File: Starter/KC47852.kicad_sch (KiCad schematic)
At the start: 49 parts, among them J1 AudioJack, J2 Speaker, J3 UART1, J4 Pot, J6 GND, J7 DACOUT, SW1 UP, SW2 LEFT, SW3 DOWN, SW4 RGHT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

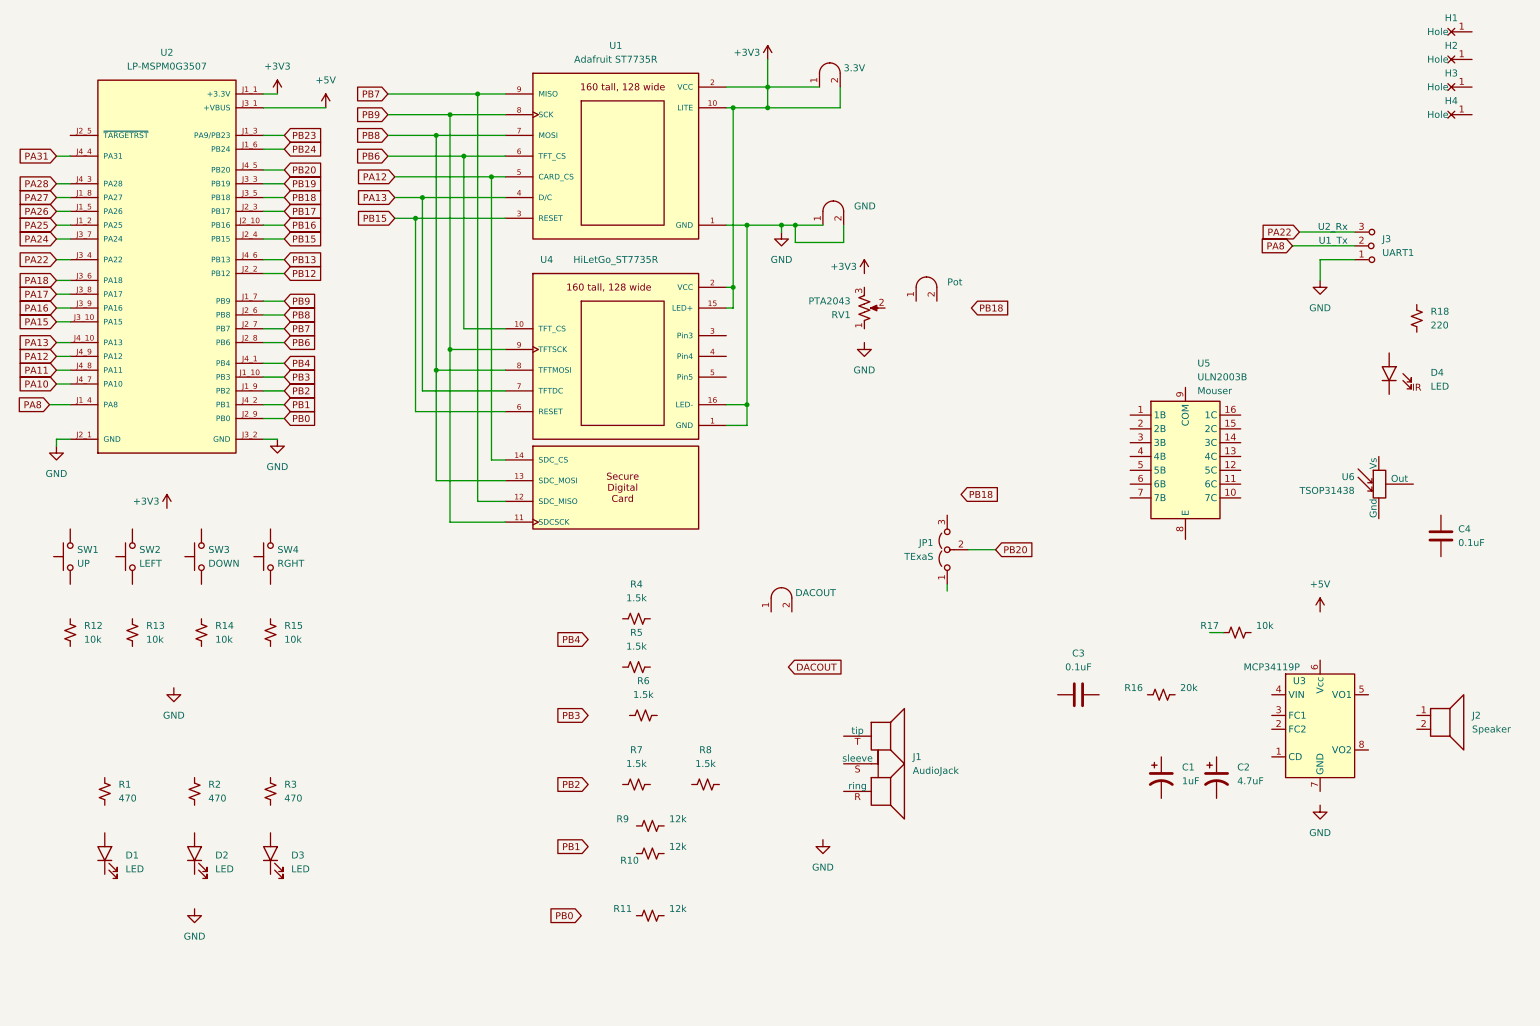
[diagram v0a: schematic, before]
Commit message: Wired LEDs, Switches, DAC, and Jumper
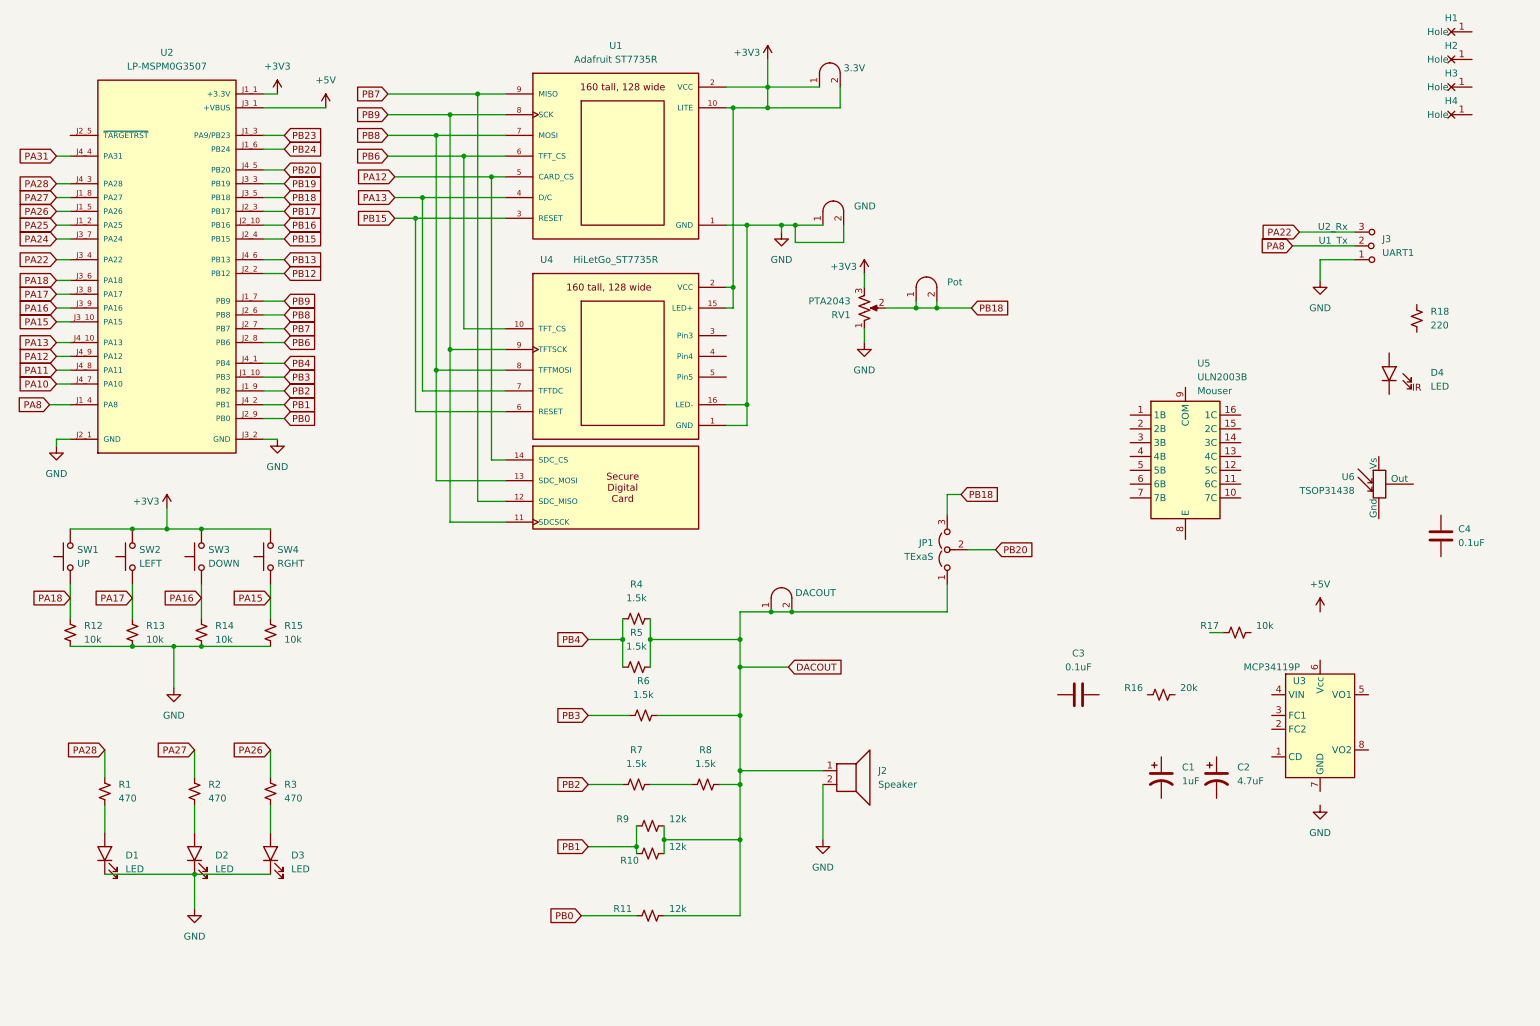
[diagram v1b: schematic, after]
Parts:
- removed J1: AudioJack, ECE319K:Jack_3.5mm_CUI_SJ1-3523N_Horizontal, symbol ECE319K:HeadphoneJack
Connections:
- net +3V3: now also RV1.3, SW1.2, SW2.2, SW3.2, SW4.2
- net DACOUT: now also J2.1, J7.1 (A), J7.2 (B), JP1.1 (A), R10.1, R11.1, R4.1, R5.1, R6.1, R8.1, R9.1
- net GND: now also D1.1 (K), D2.1 (K), D3.1 (K), J2.2, R12.2, R13.2, R14.2, R15.2, RV1.1
- net PA15: now also R15.1, SW4.1
- net PA16: now also R14.1, SW3.1
- net PA17: now also R13.1, SW2.1
- net PA18: now also R12.1, SW1.1
- net PA26: now also R3.1
- net PA27: now also R2.1
- net PA28: now also R1.1
- net PB0: now also R11.2
- net PB1: now also R10.2, R9.2
- net PB18: now also J4.1 (A), J4.2 (B), JP1.3 (B), RV1.2
- net PB2: now also R7.2
- net PB3: now also R6.2
- net PB4: now also R4.2, R5.2
- net at R7.1: now also R8.2
- net at R1.2: now also D1.2 (A)
- net at D3.2 (A): now also R3.2
- net at D2.2 (A): now also R2.2
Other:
- moved on the sheet: J2

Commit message: 319H Components
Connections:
- net +3V3: now also C4.1, U6.2 (Vs)
- net +5V: now also R18.1, U3.6 (Vcc)
- net GND: now also U3.7 (GND), U5.8 (E)
- net PA22: now also U6.3 (Out)
- net PA8: now also U5.1 (1B)
- net at C4.2: now also U6.1 (Gnd)
- net at D4.1 (K): now also U5.16 (1C)
- net at D4.2 (A): now also R18.2
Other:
- moved on the sheet: C4, D4, R18

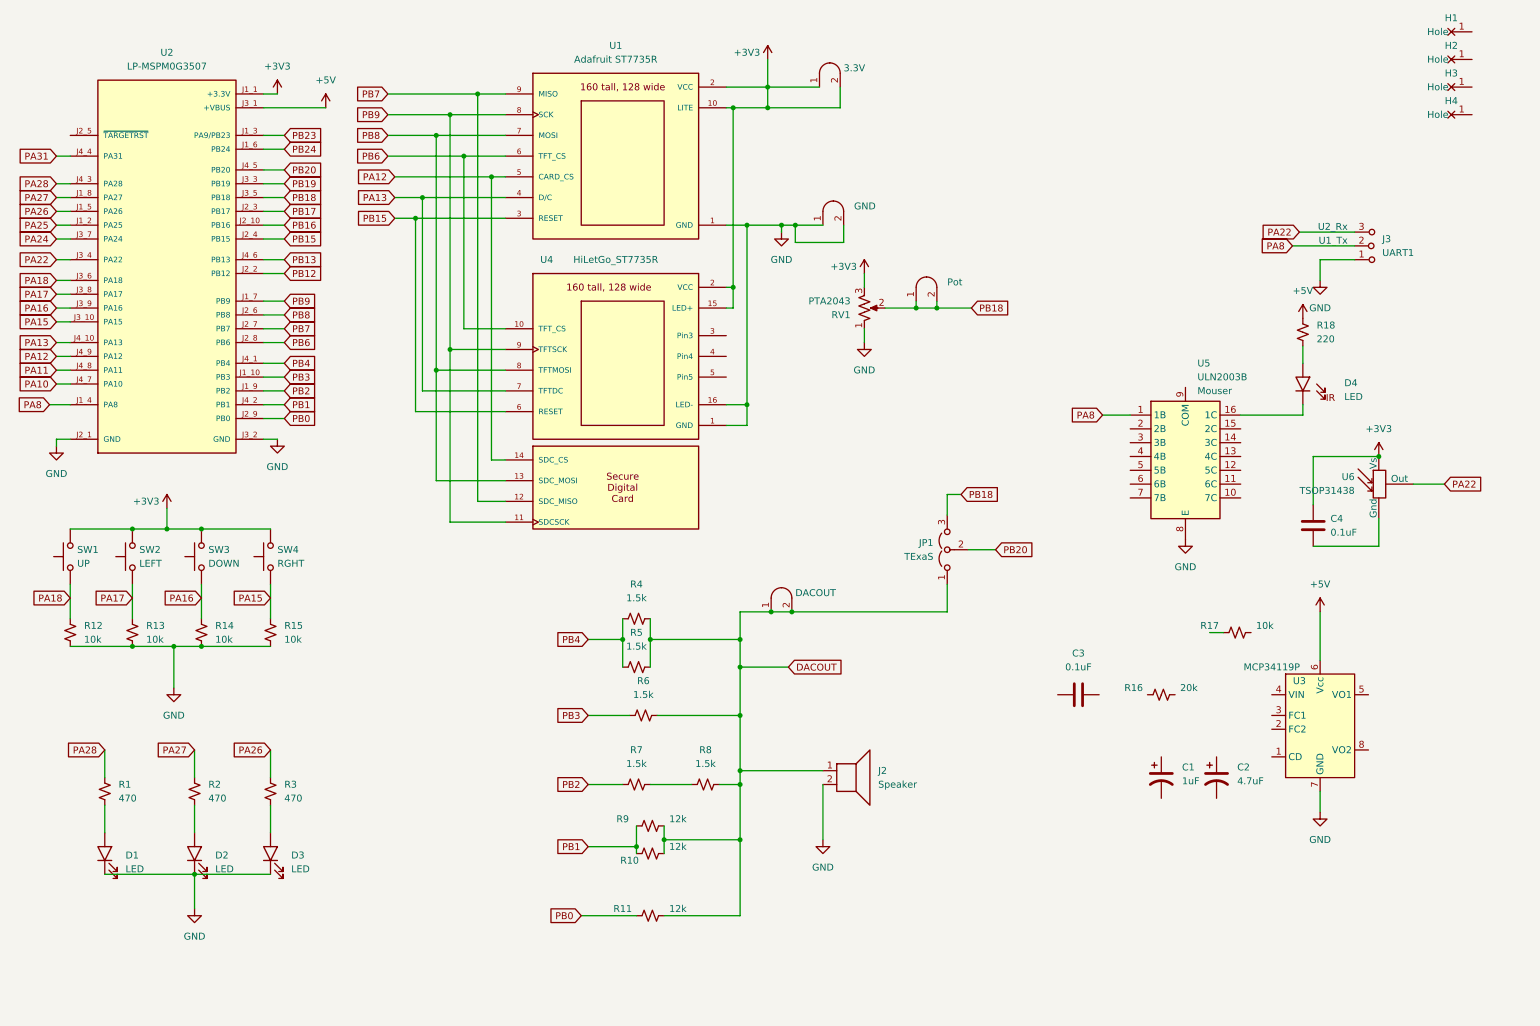
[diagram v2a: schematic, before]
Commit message: Wired audio amplifier. Referenced page 8 of Datasheet. PLEASE DOUBLE CHECK WORK
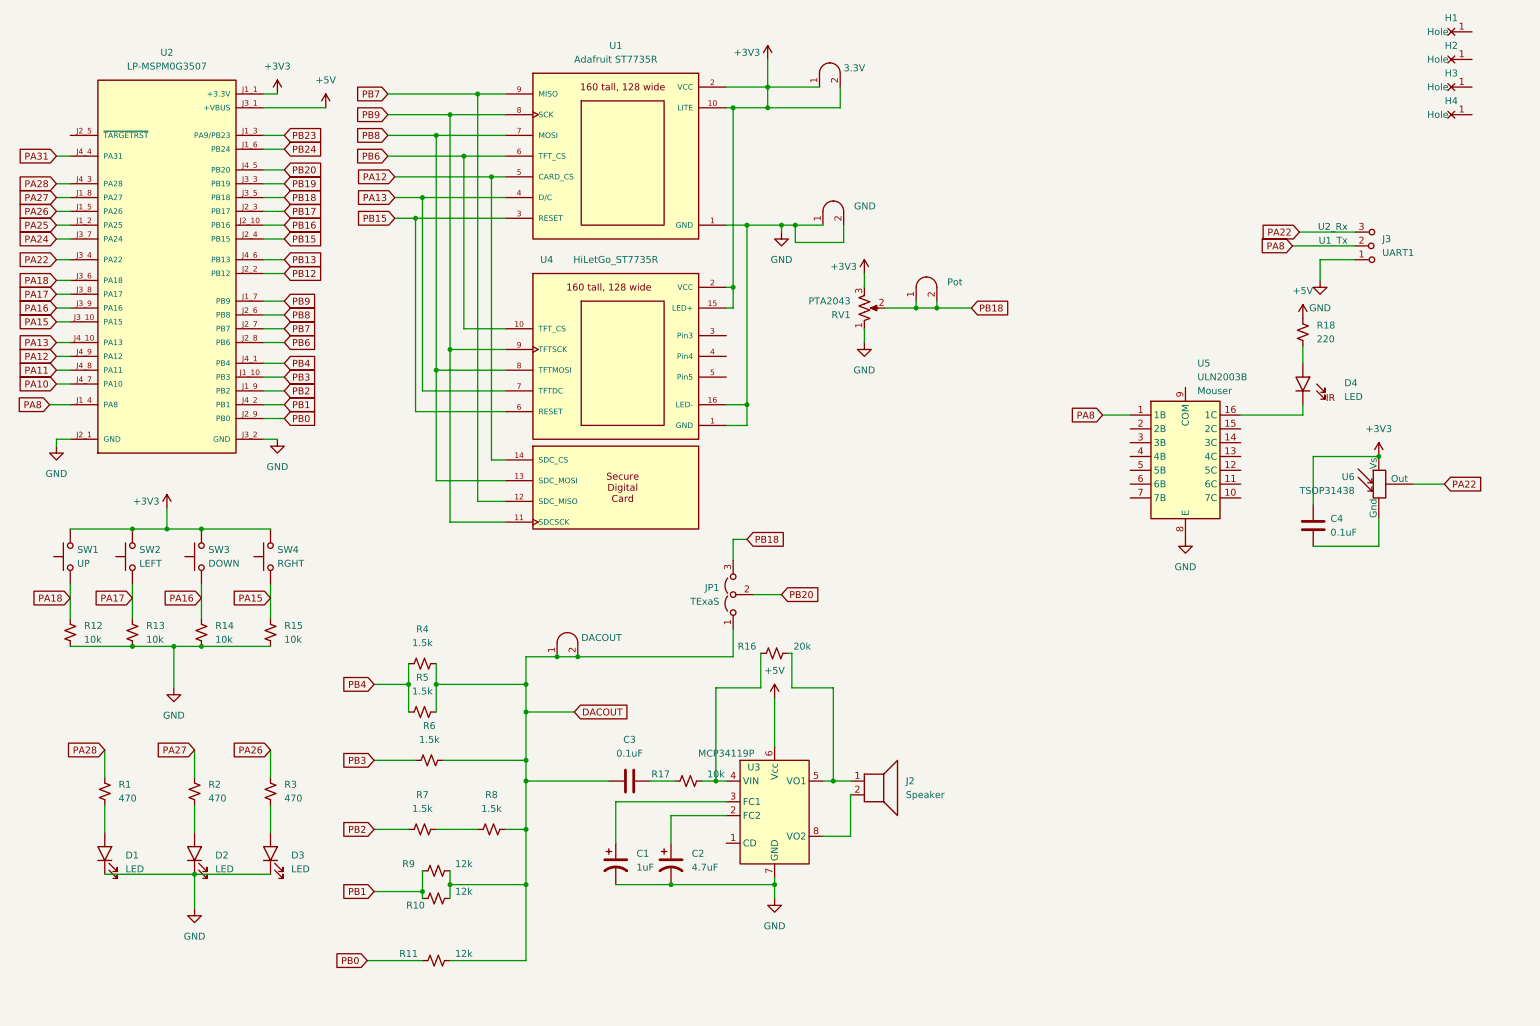
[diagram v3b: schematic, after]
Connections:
- net DACOUT: now also C3.1; no longer J2.1
- net GND: now also C1.2, C2.2; no longer J2.2
- net at U3.2 (FC2): now also C2.1
- net at U3.3 (FC1): now also C1.1
- net at U3.4 (VIN): now also R16.2, R17.1
- net at U3.5 (VO1): now also J2.1, R16.1
- net at U3.8 (VO2): now also J2.2
- net at R17.2: now also C3.2
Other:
- moved on the sheet: C1, C2, C3, J2, JP1, R10, R11, R16, R17, R4, R5, R6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

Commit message: Reformatting and added cross-board wiring as well as IMU
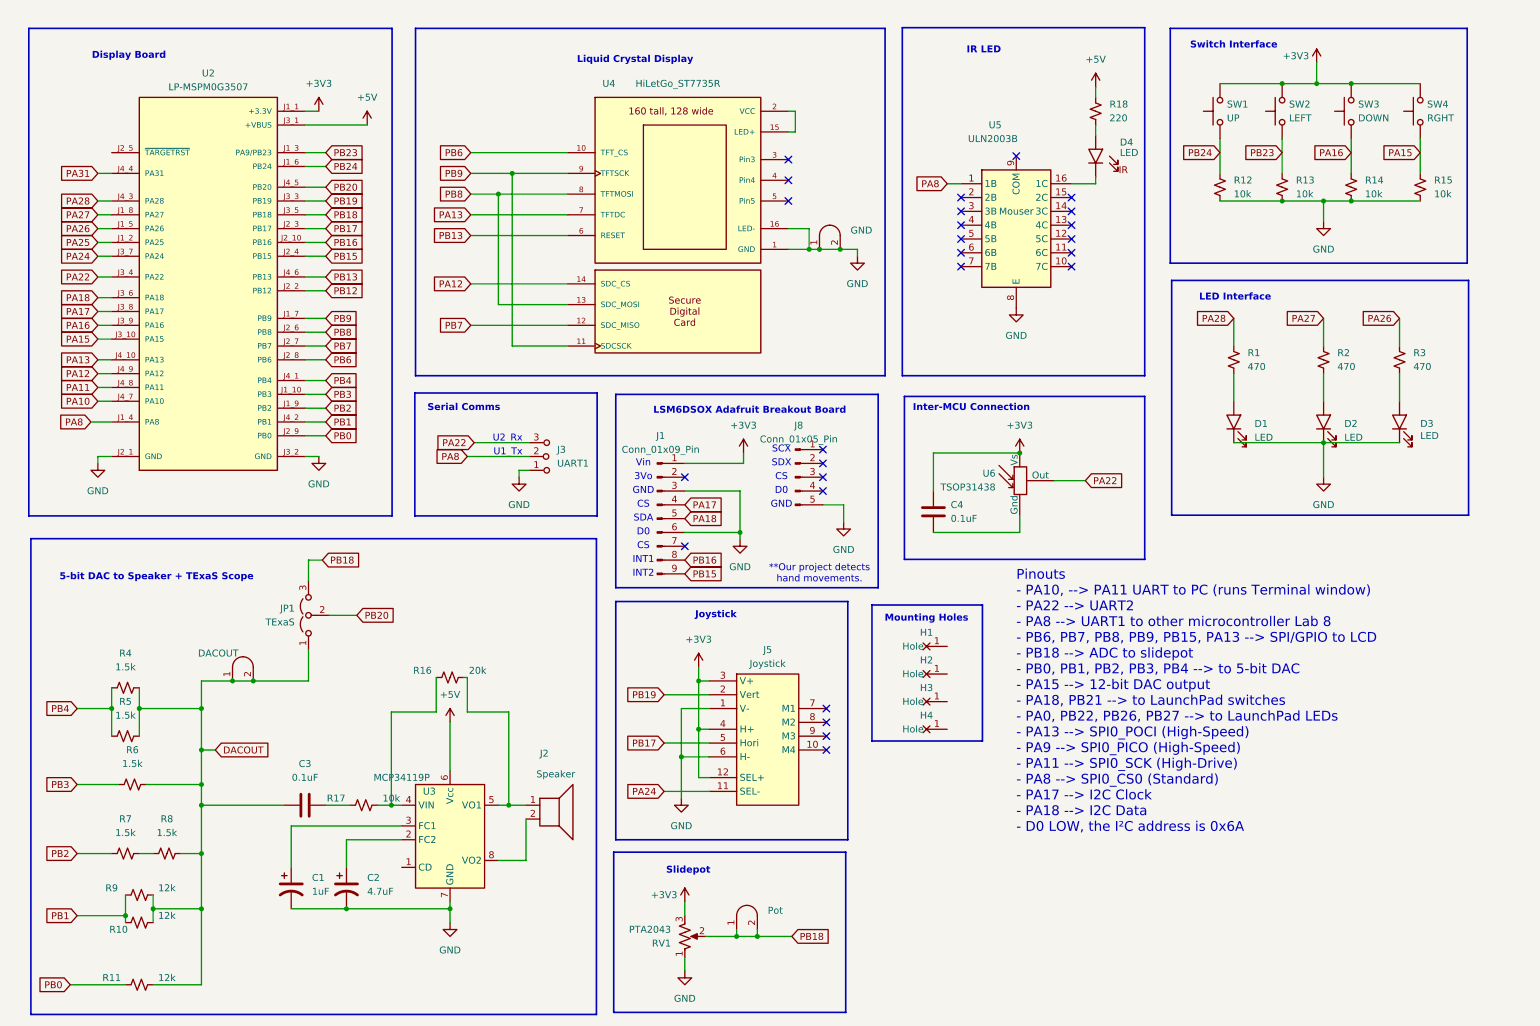
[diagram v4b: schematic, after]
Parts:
- removed TP1: 3.3V, ECE319K:Testpoint_1x02_P2.54mm, symbol ECE319K:Testpoint
- removed U1: Adafruit ST7735R, ECE319K:adafruit_st7735r, symbol ECE319K:Adafruit_ST7735R
- added J1: Conn_01x09_Pin, symbol Connector:Conn_01x09_Pin
- added J5: Joystick, ECE319K:SparkfunJoystick, symbol ECE319H:Joystick_Sparkfun_COM-09032
- added J8: Conn_01x05_Pin, symbol Connector:Conn_01x05_Pin
- U2: symbol ECE319K:LP-MSPM0G3507 -> ECE319H:LP-MSPM0G3507
- U4: symbol ECE319K:HiLetGo_ST7735R -> ECE319H:HiLetGo_ST7735R
- U5: footprint ECE319K:DIP-16_W7.62mm -> ECE319H:DIP-16_W7.62mm; symbol ECE319K:ULN2003B -> ECE319H:ULN2003B
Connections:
- net +3V3: now also J1.1 (Pin_1), J5.12 (SEL+), J5.3 (V+), J5.4 (H+); no longer U4.15 (LED+), U4.2 (VCC)
- net GND: now also J1.3 (Pin_3), J1.6 (Pin_6), J5.1 (V-), J5.6 (H-), J8.5 (Pin_5)
- net PA17: now also J1.4 (Pin_4); no longer R13.1, SW2.1
- net PA18: now also J1.5 (Pin_5); no longer R12.1, SW1.1
- net PA24: now also J5.11 (SEL-)
- net PB13: now also U4.6 (RESET)
- net PB15: now also J1.9 (Pin_9); no longer U4.6 (RESET)
- net PB16: now also J1.8 (Pin_8)
- net PB17: now also J5.5 (Hori)
- net PB19: now also J5.2 (Vert)
- net PB23: now also R13.1, SW2.1
- net PB24: now also R12.1, SW1.1
- new net: U4.15 (LED+), U4.2 (VCC)
- no-connect marks 0 -> 26
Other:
- note added: "**Our project detects hand movements."
- note added: "3Vo"
- note added: "5-bit DAC to Speaker + TExaS Scope"
- note added: "CS"
- note added: "D0"
- note added: "Display Board"
- note added: "GND"
- note added: "INT1"
- note added: "INT2"
- note added: "IR LED"
- note added: "Inter-MCU Connection"
- note added: "Joystick"
- note added: "LED Interface"
- note added: "LSM6DSOX Adafruit Breakout Board"
- note added: "Liquid Crystal Display"
- note added: "Mounting Holes"
- note added: "Pinouts - PA10, --> PA11 UART to PC (runs Terminal window) - PA22 --> UART2 - PA8 --> UART1 to other microcontroller Lab 8 - PB6, PB7, PB8, PB9, PB15, PA13 --> SPI/GPIO to LCD - PB18 --> ADC to slidepot - PB0, PB1, PB2, PB3, PB4 --> to 5-bit DAC - PA15 --> 12-bit DAC output - PA18, PB21 --> to LaunchPad switches - PA0, PB22, PB26, PB27 --> to LaunchPad LEDs - PA13 --> SPI0_POCI (High-Speed) - PA9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"
- note added: "SCX"
- note added: "SDA"
- note added: "SDX"
- note added: "Serial Comms"
- note added: "Slidepot"
- note added: "Switch Interface"
- note added: "Vin"
- moved on the sheet: C1, C2, C3, C4, D1, D2, D3, D4, H1, H2, H3, H4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

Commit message: Minor changes!
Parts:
- J1: footprint (none) -> Connector_PinHeader_2.54mm:PinHeader_1x09_P2.54mm_Vertical
- J8: footprint (none) -> Connector_PinHeader_2.54mm:PinHeader_1x05_P2.54mm_Vertical
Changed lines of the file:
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@@
 			)
 		)
-		(property "Footprint" ""
+		(property "Footprint" "Connector_PinHeader_2.54mm:PinHeader_1x05_P2.54mm_Vertical"
 			(at 156.21 97.155 0)
 			(effects
@@
 		)
 		(property "Description" "Generic connector, single row, 01x05, script generated"
+			(at 156.21 97.155 0)
+			(effects
+				(font
+					(size 1.27 1.27)
+				)
+				(hide yes)
+			)
+		)
+		(property "Mouser #" ""
+			(at 156.21 97.155 0)
+			(effects
+				(font
+					(size 1.27 1.27)
+				)
+				(hide yes)
+			)
+		)
+		(property "Mouser Link" ""
+			(at 156.21 97.155 0)
+			(effects
+				(font
+					(size 1.27 1.27)
+				)
+				(hide yes)
+			)
+		)
+		(property "JLCPCB #" ""
 			(at 156.21 97.155 0)
 			(effects
@@
 			)
 		)
-		(property "Footprint" ""
+		(property "Footprint" "Connector_PinHeader_2.54mm:PinHeader_1x09_P2.54mm_Vertical"
 			(at 130.81 104.775 0)
 			(effects
@@
 			(at 130.81 104.775 0)
 			(effects
+				(font
+					(size 1.27 1.27)
+				)
+				(hide yes)
+			)
+		)
+		(property "Mouser #" ""
+			(at 130.81 104.775 0)
+			(effects
+				(font
+					(size 1.27 1.27)
+				)
+				(hide yes)
+			)
+		)
+		(property "Mouser Link" ""
+			(at 130.81 104.775 0)
+			(effects
+				(font
+					(size 1.27 1.27)
+				)
+				(hide yes)
+			)
+		)
+		(property "JLCPCB #" ""
+			(at 130.81 104.775 0)
+			(effects

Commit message: Minor edits V2!
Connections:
- no-connect marks 26 -> 27
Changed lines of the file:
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@@
+	)
+	(no_connect
+		(at 83.82 168.91)
 	)
 	(no_connect
